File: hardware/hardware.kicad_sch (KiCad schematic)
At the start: 48 parts, among them J1 USB_C_Receptacle_USB2.0_16P, J2 Conn_01x02_Pin, J3 C-OBD-II-16M, J4 Conn_01x06, J5 Conn_01x02_Pin, J6 Conn_01x06, J8 Screw_Terminal_01x02, SW3 Reset, SW4 Boot, U1 ESP32-S3-WROOM-1U-N16R8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

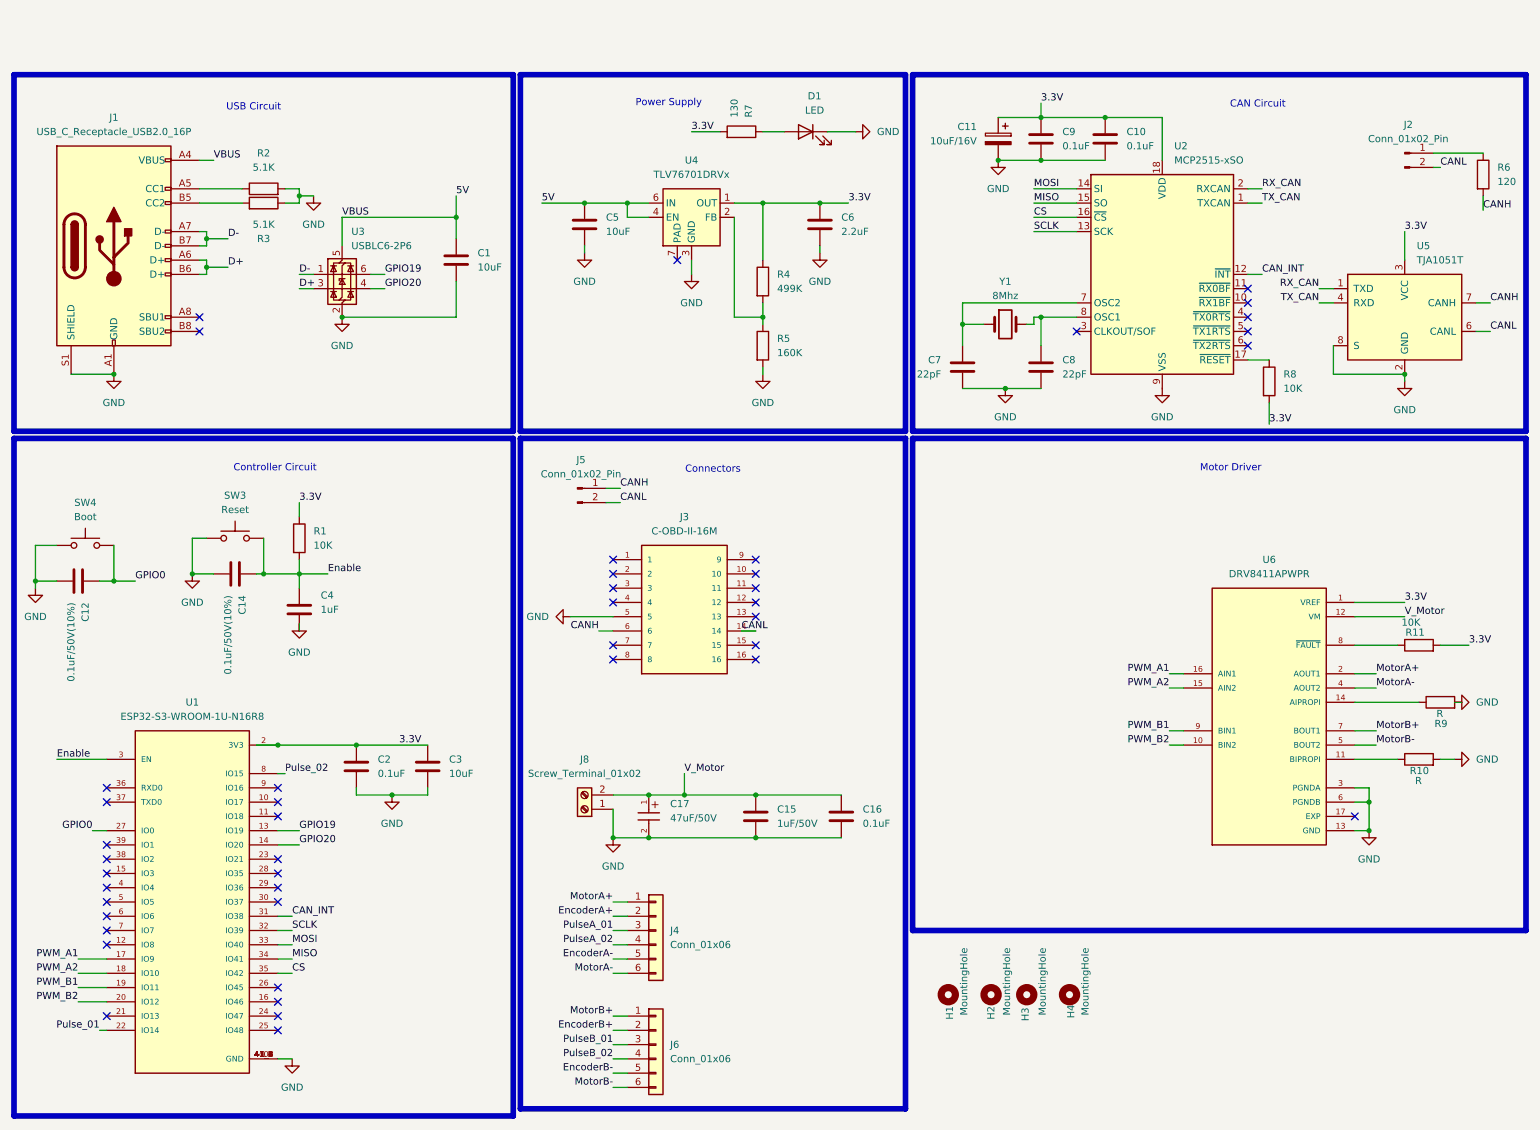
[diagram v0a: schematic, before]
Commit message: Added Leds and moved from 2 to 4 layers pcb
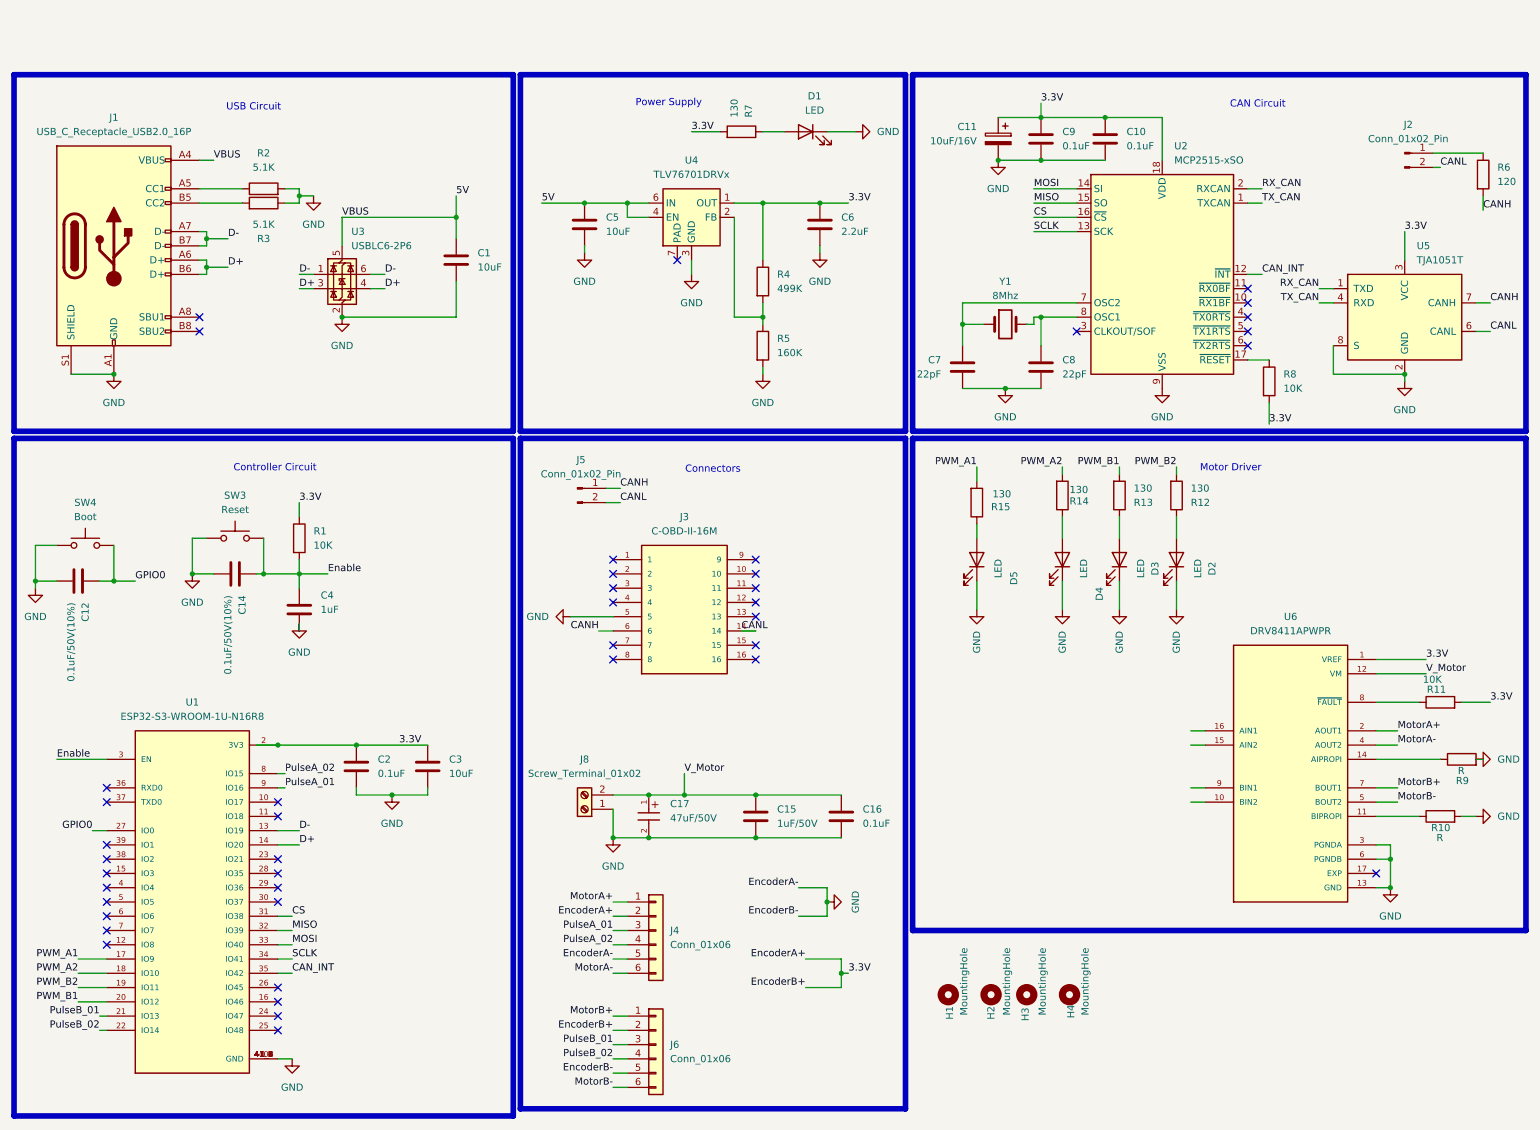
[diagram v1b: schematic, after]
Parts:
- added D2, D3, D4, D5: LED, LED_SMD:LED_0805_2012Metric_Pad1.15x1.40mm_HandSolder, symbol Device:LED
- added R12, R13, R14, R15: 130, Resistor_SMD:R_0402_1005Metric, symbol Device:R
- C1: footprint Capacitor_SMD:C_0805_2012Metric_Pad1.18x1.45mm_HandSolder -> Capacitor_SMD:C_0402_1005Metric
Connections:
- net EncoderA+ is gone; now on net 3.3V: J4.2 (Pin_2)
- net EncoderA- is gone; now on net GND: J4.5 (Pin_5)
- net EncoderB+ is gone; now on net 3.3V: J6.2 (Pin_2)
- net EncoderB- is gone; now on net GND: J6.5 (Pin_5)
- net GPIO19 is gone; now on net D-: U1.13 (IO19), U3.6 (I/O1)
- net GPIO20 is gone; now on net D+: U1.14 (IO20), U3.4 (I/O2)
- net Pulse_01 is gone; now on net PulseB_02: U1.22 (IO14)
- net Pulse_02 is gone; now on net PulseA_02: U1.8 (IO15)
- net CAN_INT: now also U1.35 (IO42); no longer U1.31 (IO38)
- net CS: now also U1.31 (IO38); no longer U1.35 (IO42)
- net GND: now also D2.1 (K), D3.1 (K), D4.1 (K), D5.1 (K)
- net MISO: now also U1.32 (IO39); no longer U1.34 (IO41)
- net PWM_A1: now also R15.2; no longer U6.16 (AIN1)
- net PWM_A2: now also R14.2; no longer U6.15 (AIN2)
- net PWM_B1: now also U1.20 (IO12), R13.2; no longer U1.19 (IO11), U6.9 (BIN1)
- net PWM_B2: now also U1.19 (IO11), R12.2; no longer U1.20 (IO12), U6.10 (BIN2)
- net PulseA_01: now also U1.9 (IO16)
- net PulseB_01: now also U1.21 (IO13)
- net SCLK: now also U1.34 (IO41); no longer U1.32 (IO39)
- new net: D2.2 (A), R12.1
- new net: D5.2 (A), R15.1
- new net: D3.2 (A), R13.1
- new net: D4.2 (A), R14.1
- no-connect marks 45 -> 43
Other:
- moved on the sheet: R10, R11, R9, U6

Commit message: Changed motor driver IC from DRV8411 to DRV8871 PCB updated as well added manufacture values in schematics
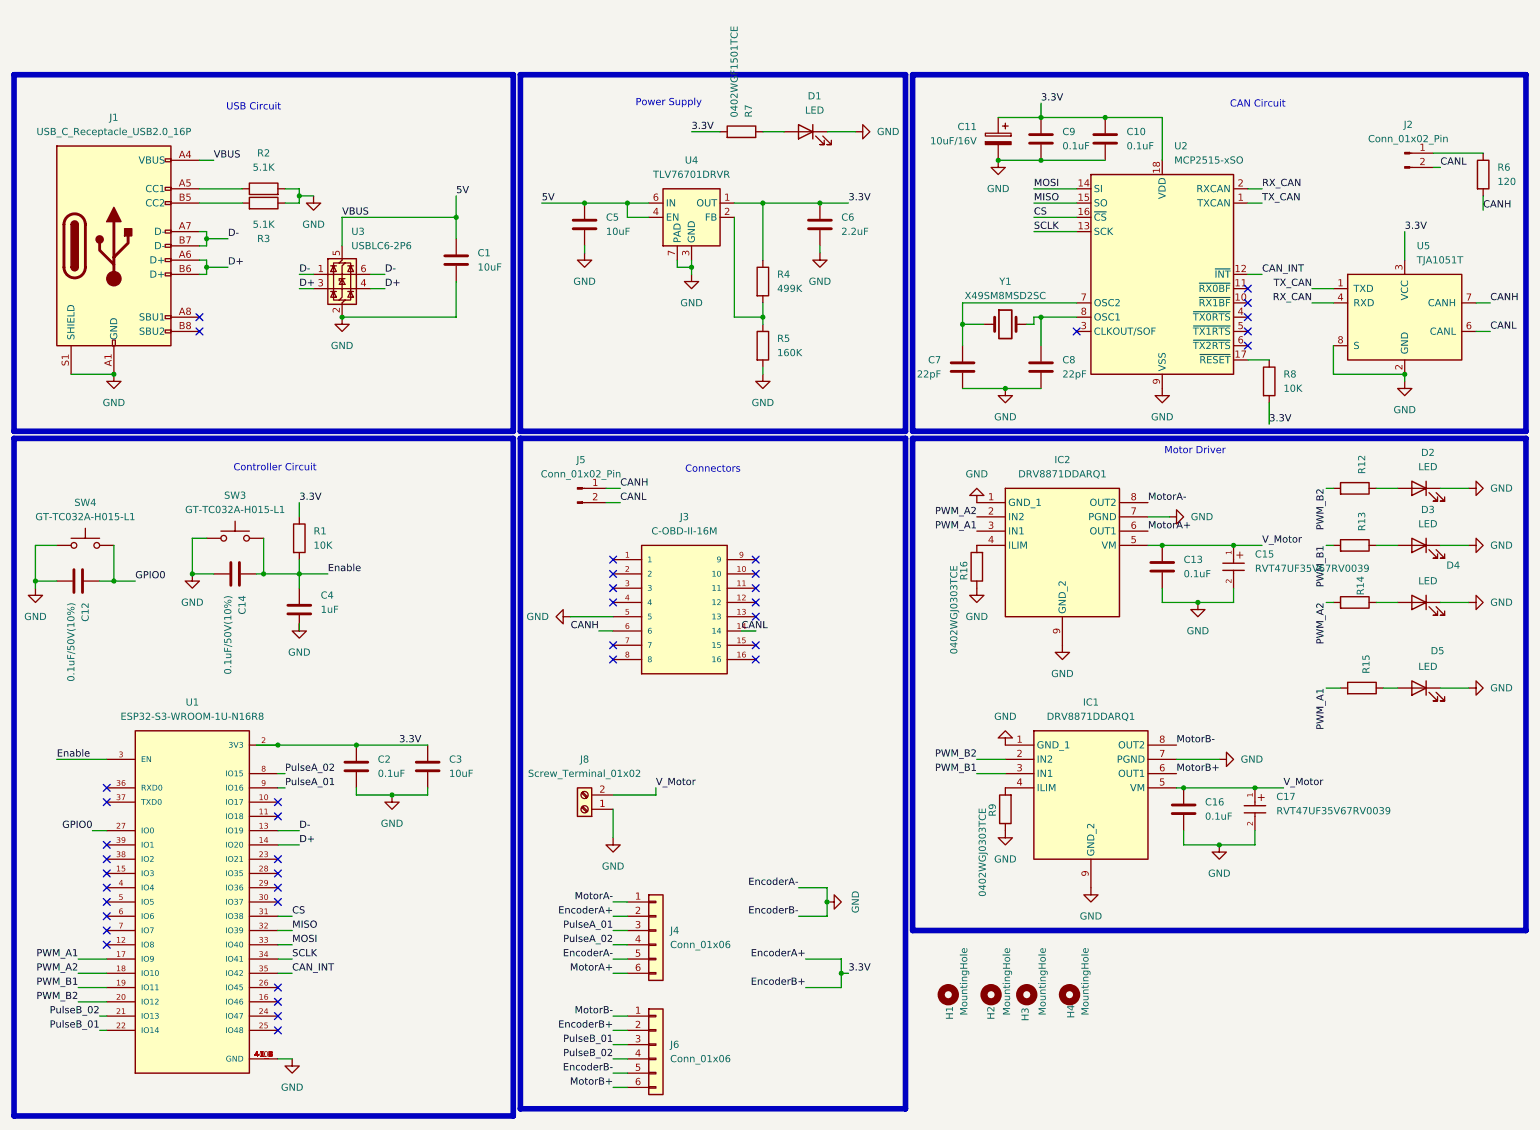
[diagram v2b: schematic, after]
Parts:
- removed C15: 1uF/50V, Capacitor_SMD:C_0805_2012Metric, symbol Device:C
- removed R10: R, Resistor_SMD:R_0201_0603Metric, symbol Device:R
- removed R11: 10K, Resistor_SMD:R_0201_0603Metric, symbol Device:R
- removed U6: DRV8411APWPR, DRV8411APWPR:IC_DRV8411APWPR, symbol DRV8411APWPR:DRV8411APWPR
- added C13: 0.1uF, Capacitor_SMD:C_0402_1005Metric, symbol Device:C
- added C15: RVT47UF35V67RV0039, Capacitor_SMD:CP_Elec_3x5.4, symbol WCAP-ASLI_6.3X7.7:WCAP-ASLI_6.3X7.7
- added IC1, IC2: DRV8871DDARQ1, SOIC127P600X170-9N, symbol DRV8871DDARQ1:DRV8871DDARQ1
- added R16: 0402WGJ0303TCE, Resistor_SMD:R_0402_1005Metric, symbol Device:R
- C16: footprint Capacitor_SMD:C_0201_0603Metric -> Capacitor_SMD:C_0402_1005Metric
- C17: value 47uF/50V -> RVT47UF35V67RV0039; footprint WCAP-ASLI_6.3X7.7:WCAP-ASLI_6.3X7.7_DXL_ -> Capacitor_SMD:CP_Elec_3x5.4
- R12, R13, R14, R15, R7: value 130 -> 0402WGF1501TCE
- R9: value R -> 0402WGJ0303TCE; footprint Resistor_SMD:R_0201_0603Metric -> Resistor_SMD:R_0402_1005Metric
- SW3: value Reset -> GT-TC032A-H015-L1
- SW4: value Boot -> GT-TC032A-H015-L1
- U4: value TLV76701DRVx -> TLV76701DRVR
- Y1: value 8Mhz -> X49SM8MSD2SC
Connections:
- net GND: now also R9.1, U4.7 (PAD), C13.2, C15.2, IC1.1 (GND_1), IC1.7 (PGND), IC1.9 (GND_2), IC2.1 (GND_1), IC2.7 (PGND), IC2.9 (GND_2), R16.1; no longer R9.2
- net MotorA+: now also J4.6 (Pin_6), IC2.6 (OUT1); no longer J4.1 (Pin_1)
- net MotorA-: now also J4.1 (Pin_1), IC2.8 (OUT2); no longer J4.6 (Pin_6)
- net MotorB+: now also J6.6 (Pin_6), IC1.6 (OUT1); no longer J6.1 (Pin_1)
- net MotorB-: now also J6.1 (Pin_1), IC1.8 (OUT2); no longer J6.6 (Pin_6)
- net PWM_A1: now also IC2.3 (IN1)
- net PWM_A2: now also IC2.2 (IN2)
- net PWM_B1: now also U1.19 (IO11), IC1.3 (IN1); no longer U1.20 (IO12)
- net PWM_B2: now also U1.20 (IO12), IC1.2 (IN2); no longer U1.19 (IO11)
- net PulseB_01: now also U1.22 (IO14); no longer U1.21 (IO13)
- net PulseB_02: now also U1.21 (IO13); no longer U1.22 (IO14)
- net RX_CAN: now also U5.4 (RXD); no longer U5.1 (TXD)
- net TX_CAN: now also U5.1 (TXD); no longer U5.4 (RXD)
- net V_Motor: now also C13.1, C15.1, IC1.5 (VM), IC2.5 (VM)
- new net: IC2.4 (ILIM), R16.2
- new net: IC1.4 (ILIM), R9.2
- no-connect marks 43 -> 41
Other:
- moved on the sheet: C16, C17, D2, D3, D4, D5, R12, R13, R14, R15

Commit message: version 1
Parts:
- C13, C16: value 0.1uF -> CL05B104KO5NNNC
- C15, C17: footprint Capacitor_SMD:CP_Elec_3x5.4 -> Capacitor_SMD:CP_Elec_6.3x5.4
- C6: value 2.2uF -> CL05A225MQ5NSNC
- J1: value USB_C_Receptacle_USB2.0_16P -> TYPE-C-31-M-12
- R4: value 499K -> 0402WGJ0513TCE
- R5: value 160K -> 0402WGJ0163TCE
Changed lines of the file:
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@@
 			)
 		)
-		(property "Value" "160K"
+		(property "Value" "0402WGJ0163TCE"
 			(at 149.86 62.2299 0)
 			(effects
@@
 			)
 		)
-		(property "Footprint" "Capacitor_SMD:CP_Elec_3x5.4"
+		(property "Footprint" "Capacitor_SMD:CP_Elec_6.3x5.4"
 			(at 234.95 144.78 0)
 			(effects
@@
 			)
 		)
-		(property "Value" "2.2uF"
+		(property "Value" "CL05A225MQ5NSNC"
 			(at 161.29 40.6399 0)
 			(effects
@@
 			)
 		)
-		(property "Value" "0.1uF"
+		(property "Value" "CL05B104KO5NNNC"
 			(at 222.25 101.5999 0)
 			(effects
@@
 			)
 		)
-		(property "Value" "0.1uF"
+		(property "Value" "CL05B104KO5NNNC"
 			(at 226.06 144.7799 0)
 			(effects
@@
 			)
 		)
-		(property "Value" "499K"
+		(property "Value" "0402WGJ0513TCE"
 			(at 149.86 50.7999 0)
 			(effects
@@
 			)
 		)
-		(property "Footprint" "Capacitor_SMD:CP_Elec_3x5.4"
+		(property "Footprint" "Capacitor_SMD:CP_Elec_6.3x5.4"
 			(at 231.14 101.6 0)
 			(effects
@@
 			)
 		)
-		(property "Value" "USB_C_Receptacle_USB2.0_16P"
+		(property "Value" "TYPE-C-31-M-12"
 			(at 31.75 22.86 0)
 			(effects
